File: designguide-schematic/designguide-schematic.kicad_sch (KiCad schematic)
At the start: 93 parts, among them J1 HRO_TYPE-C-31-M-14, J2 UDB, J3 Battery, J4 Battery, J5 Thermistor, J6 Battery, J7 SWD_TC2030, J8 SWD_TC2030, Q1 AO3401A, Q2 2N7002, Q3 AO3401A, Q4 2N7002, SW1 PWR, SW2 PWR, SW3 RESET, SW4 RESET, SW5 Keyswitch, SW6 Keyswitch, SW7 Keyswitch, SW8 Keyswitch, U1 SRV05-4, U10 TXB0101, U2 TP4056, U3 BQ24075, U4 DW01A, U5 FS8205, U6 XC6206PxxxMR, U7 nRF52840_holyiot_18010, U8 nRF52840_moko_mk08, U9 MAX17048

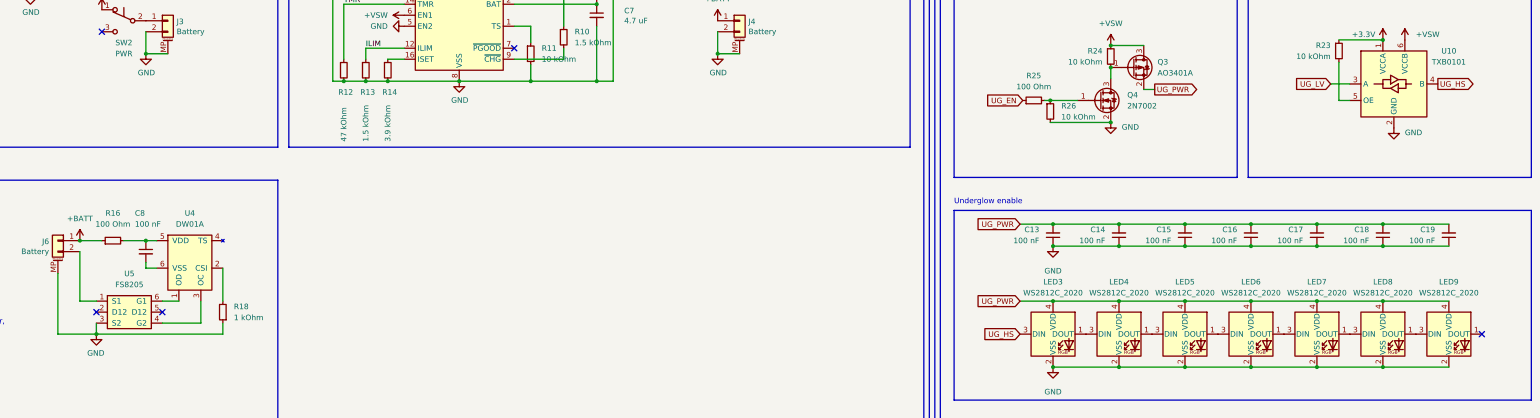
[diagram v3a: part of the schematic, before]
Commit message: fixed missing connection in batt protections, add disclaimer to readme
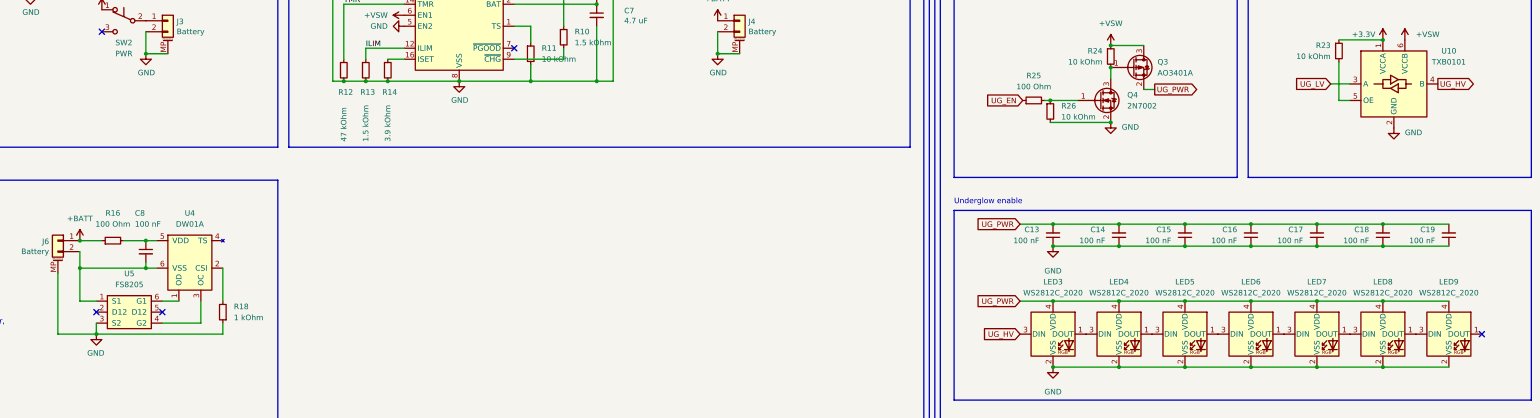
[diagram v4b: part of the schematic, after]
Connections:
- net at C8.2, U4.6 (VSS): now also J6.2 (Pin_2), U5.1 (S1)
- net UG_HS renamed UG_HV
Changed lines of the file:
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@@
   (junction (at 36.83 256.54) (diameter 0) (color 0 0 0 0)
   )
+  (junction (at 80.01 185.42) (diameter 0) (color 0 0 0 0)
+  )
   (junction (at 335.28 193.04) (diameter 0) (color 0 0 0 0)
   )
@@
   )
   (junction (at 227.33 110.49) (diameter 0) (color 0 0 0 0)
+  )
+  (junction (at 95.25 185.42) (diameter 0) (color 0 0 0 0)
   )
   (junction (at 151.13 142.24) (diameter 0.9144) (color 0 0 0 0)
@@
     (stroke (width 0) (type default) (color 0 0 0 0))
   )
+  (wire (pts (xy 80.01 185.42) (xy 95.25 185.42))
+    (stroke (width 0) (type default) (color 0 0 0 0))
+  )
   (polyline (pts (xy 281.94 215.9) (xy 415.29 215.9))
     (stroke (width 0) (type solid) (color 0 0 0 0))
@@
     (stroke (width 0) (type default) (color 0 0 0 0))
   )
+  (wire (pts (xy 80.01 185.42) (xy 80.01 193.04))
+    (stroke (width 0) (type default) (color 0 0 0 0))
+  )
   (wire (pts (xy 350.52 180.34) (xy 365.76 180.34))
     (stroke (width 0) (type default) (color 0 0 0 0))
@@
     (stroke (width 0) (type default) (color 0 0 0 0))
   )
-  (wire (pts (xy 80.01 181.61) (xy 80.01 193.04))
+  (wire (pts (xy 80.01 181.61) (xy 80.01 185.42))
     (stroke (width 0) (type default) (color 0 0 0 0))
   )
@@
     )
   )
-  (global_label "UG_HS" (shape output) (at 393.7 142.875 0) (fields_autoplaced)
-    (effects (font (size 1.27 1.27)) (justify left))
-    (property "Intersheet References" "${INTERSHEET_REFS}" (id 0) (at 402.2212 142.7956 0)
+  (global_label "UG_HV" (shape output) (at 393.7 142.875 0) (fields_autoplaced)
+    (effects (font (size 1.27 1.27)) (justify left))
+    (property "Intersheet References" "${INTERSHEET_REFS}" (id 0) (at 402.1002 142.7956 0)
       (effects (font (size 1.27 1.27)) (justify left) hide)
     )
@@
     )
   )
-  (global_label "UG_HS" (shape input) (at 297.18 200.66 180) (fields_autoplaced)
-    (effects (font (size 1.27 1.27)) (justify right))
-    (property "Intersheet References" "${INTERSHEET_REFS}" (id 0) (at 288.6588 200.5806 0)
-      (effects (font (size 1.27 1.27)) (justify right) hide)
-    )
+  (global_label "UG_HV" (shape input) (at 297.18 200.66 180) (fields_autoplaced)
+    (effects (font (size 1.27 1.27)) (justify right))
+    (property "Intersheet References" "${INTERSHEET_REFS}" (id 0) (at 288.7798 200.5806 0)
+      (effects (font (size 1.27 1.27)) (justify right) hide)
+    )

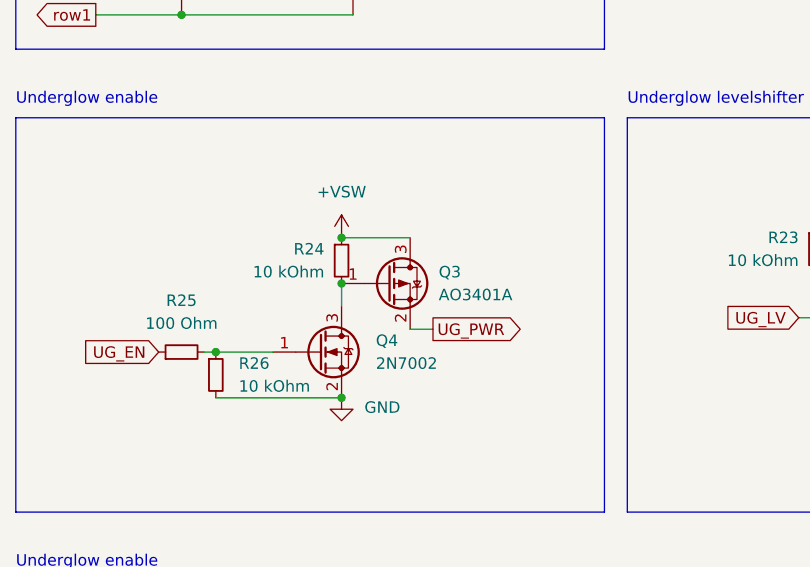
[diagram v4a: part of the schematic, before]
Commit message: fixed wrong rotation of p-ch FET in underglow supply
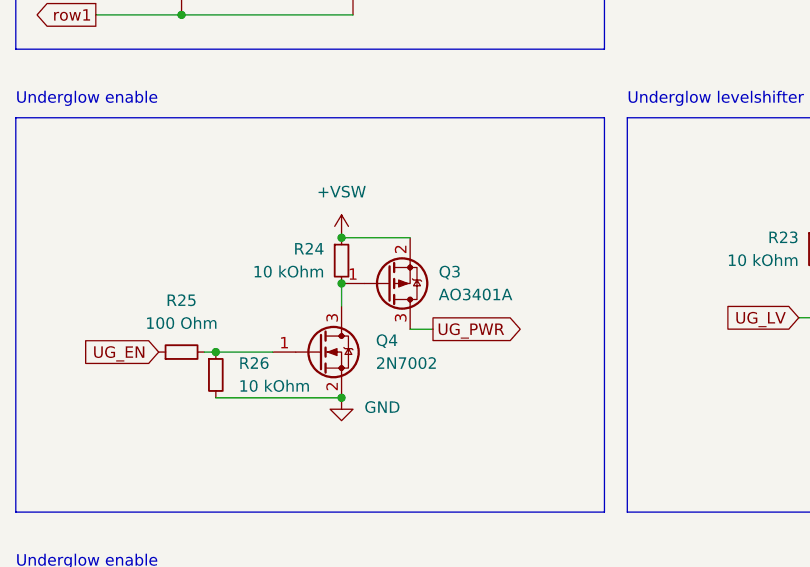
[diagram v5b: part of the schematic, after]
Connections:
- net +VSW: now also Q3.2 (S); no longer Q3.3 (D)
- net UG_PWR: now also Q3.3 (D); no longer Q3.2 (S)
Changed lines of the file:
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@@
   (junction (at 27.94 67.31) (diameter 0.9144) (color 0 0 0 0)
   )
+  (junction (at 318.135 139.065) (diameter 0) (color 0 0 0 0)
+  )
   (junction (at 350.52 175.26) (diameter 0) (color 0 0 0 0)
   )
@@
   )
   (junction (at 59.055 248.92) (diameter 0) (color 0 0 0 0)
-  )
-  (junction (at 318.135 139.065) (diameter 0) (color 0 0 0 0)
   )
   (junction (at 71.12 114.3) (diameter 0) (color 0 0 0 0)
@@
     (pin "2")
   )
-  (symbol (lib_id "Transistor_FET:AO3401A") (at 323.215 139.065 0) (unit 1)
+  (symbol (lib_id "Transistor_FET:AO3401A") (at 323.215 139.065 0) (mirror x) (unit 1)
     (in_bom yes) (on_board yes) (fields_autoplaced)
     (property "Reference" "Q3" (id 0) (at 328.93 137.7949 0)
@@
       (effects (font (size 1.27 1.27)) (justify left))
     )
-    (property "Footprint" "Package_TO_SOT_SMD:SOT-23" (id 2) (at 328.295 140.97 0)
+    (property "Footprint" "Package_TO_SOT_SMD:SOT-23" (id 2) (at 328.295 137.16 0)
       (effects (font (size 1.27 1.27) italic) (justify left) hide)
     )

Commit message: fixes #9, moves the project over to KiCad 7.0 and marbastlib PCM version instead of submodule
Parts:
- J7, J8: value SWD_TC2030 -> TC2030_SWD; footprint marbastlib-various:CON_TC2030_outlined -> PCM_marbastlib-various:CON_TC2030_outlined; symbol marbastlib-various:JTAG_TC2030 -> PCM_marbastlib-various:TC2030_SWD
- LED3, LED4, LED5, LED6, LED7, LED8, LED9: value WS2812C_2020 -> WS2812_2020; footprint marbastlib-various:LED_WS2812_2020 -> PCM_marbastlib-various:LED_WS2812_2020; symbol marbastlib-various:WS2812_2020 -> PCM_marbastlib-various:WS2812_2020
- SW1, SW2: footprint marbastlib-various:SW_MSK12C02-HB -> PCM_marbastlib-various:SW_MSK12C02-HB
- SW3, SW4: footprint (none) -> PCM_marbastlib-various:SW_SPST_SKQG_WithStem
- SW5, SW6, SW7, SW8: value Keyswitch -> MX_SW_HS; footprint (none) -> PCM_marbastlib-mx:SW_MX_HS_1u; symbol Switch:SW_Push_45deg -> PCM_marbastlib-mx:MX_SW_HS
- U10: symbol marbastlib-various:TXB0101 -> PCM_marbastlib-various:TXB0101
- U2: symbol marbastlib-various:TP4056 -> PCM_marbastlib-various:TP4056
- U4: symbol marbastlib-various:DW01A -> PCM_marbastlib-various:DW01A
- U5: symbol marbastlib-various:FS8205 -> PCM_marbastlib-various:FS8205
- U7: footprint marbastlib-various:nRF52840_holyiot_18010 -> PCM_marbastlib-various:nRF52840_holyiot_18010; symbol marbastlib-various:nRF52840_holyiot_18010 -> PCM_marbastlib-various:nRF52840_holyiot_18010
- U8: footprint marbastlib-various:nRF52840_moko_mk08 -> PCM_marbastlib-various:nRF52840_moko_mk08; symbol marbastlib-various:nRF52840_moko_mk08 -> PCM_marbastlib-various:nRF52840_moko_mk08
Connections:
- net USB-Di- is gone; now on net USB-D-: U1.1 (IO1)
- net USB-Do- is gone; now on net USB-D+: U1.6 (IO4)
- net GND: no longer U7.25 (GND)
- net SCL: now also R20.1; no longer R19.1
- net SDA: now also R19.1; no longer R20.1
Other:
- moved on the sheet: C12, D3, D4, D5, D6, Q3, Q4, R19, R20, R23, R24, R25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

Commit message: Address issue #10, add ebyte e73 module, add thermistor for bq24075, rework USB filtering to follow USB specs
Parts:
- removed R3: 1 MOhm, Resistor_SMD:R_0402_1005Metric, symbol Device:R_Small
- added C12: 1u, Capacitor_SMD:C_0402_1005Metric, symbol Device:C_Small
- added C13, C14: 4u7, Capacitor_SMD:C_0402_1005Metric, symbol Device:C_Small
- added C15, C16: 12p, Capacitor_SMD:C_0402_1005Metric, symbol Device:C_Small
- added J10: TC2030_SWD, PCM_marbastlib-various:CON_TC2030_outlined, symbol PCM_marbastlib-various:TC2030_SWD
- added J7: Thermistor, Connector_JST:JST_PH_S2B-PH-K_1x02_P2.00mm_Horizontal, symbol Connector_Generic_MountingPin:Conn_01x02_MountingPin
- added L3: 10 uH, Inductor_SMD:L_0603_1608Metric, symbol Device:L_Small
- added SW5: RST, PCM_marbastlib-various:SW_SPST_SKQG_WithStem, symbol Switch:SW_Push_45deg
- added U9: nRF52840_E73-2G4M08S1C, PCM_marbastlib-various:nRF52840_E73-2G4M08S1C, symbol PCM_marbastlib-various:nRF52840_E73-2G4M08S1C
- added Y1: 32.768 KHz, Crystal:Crystal_SMD_2012-2Pin_2.0x1.2mm, symbol Device:Crystal_Small
- C1, C11, C8: value 100 nF -> 100n
- C10, C9: value 1 uF -> 1u
- C17: renamed from C12; value 100 nF -> 100n; LCSC C52923 -> (none)
- C18: renamed from C13; value 100 nF -> 100n; LCSC C52923 -> (none)
- C19: renamed from C14; value 100 nF -> 100n; LCSC C52923 -> (none)
- C2, C4: value 10 uF -> 10u
- C20: renamed from C15; value 100 nF -> 100n; LCSC C52923 -> (none)
- C21: renamed from C16; value 100 nF -> 100n; LCSC C52923 -> (none)
- C22: renamed from C17; value 100 nF -> 100n; LCSC C52923 -> (none)
- C23: renamed from C18; value 100 nF -> 100n; LCSC C52923 -> (none)
- C24: renamed from C19; value 100 nF -> 100n; LCSC C52923 -> (none)
- C3, C5, C6, C7: value 4.7 uF -> 4u7
- J3: renamed from J4; footprint Connector_JST:JST_PH_S2B-PH-K_1x02_P2.00mm_Horizontal -> PCM_marbastlib-various:Molex_Pico-EZmate_78171-0002_1x02-1MP_P1.20mm_Vertical; LCSC (none) -> C505023
- J4: renamed from J3; footprint Connector_JST:JST_PH_S2B-PH-K_1x02_P2.00mm_Horizontal -> PCM_marbastlib-various:Molex_Pico-EZmate_78171-0002_1x02-1MP_P1.20mm_Vertical; LCSC (none) -> C505023
- J6: footprint Connector_JST:JST_PH_S2B-PH-K_1x02_P2.00mm_Horizontal -> PCM_marbastlib-various:Molex_Pico-EZmate_78171-0002_1x02-1MP_P1.20mm_Vertical; LCSC (none) -> C505023
- R1, R2: value 5.1 kOhm -> 5k1
- R10: value 1.5 kOhm -> 1k5
- R11: renamed from R12; value 47 kOhm -> 47k
- R12: renamed from R13; value 1.5 kOhm -> 1k5
- R13: renamed from R14; value 3.9 kOhm -> 3k9
- R14: renamed from R15; value 5 kOhm -> 5k
- R15: renamed from R16; value 100 Ohm -> 100R
- R16: renamed from R17; value 5 kOhm -> 5k
- R17: renamed from R18; value 1 kOhm -> 1k
- R18: renamed from R19; value 5.1 kOhm -> 5k1
- R19: renamed from R20; value 5.1 kOhm -> 5k1
- R20: renamed from R21; value 806 kOhm -> 806k
- R21: renamed from R22; value 2 MOhm -> 2M
- R22: renamed from R23; value 10 kOhm -> 10k
- R23: renamed from R24; value 10 kOhm -> 10k
- R24: renamed from R25; value 100 Ohm -> 100R
- R25: renamed from R26; value 10 kOhm -> 10k
- R3: renamed from R4; value 100 kOhm -> 100k
- R4: renamed from R5; value 100 Ohm -> 100R
- R5: renamed from R6; value 1.5 kOhm -> 1k5
- R6: renamed from R7; value 1.5 kOhm -> 1k5
- R7: renamed from R8; value 10 kOhm -> 10k
- R8: renamed from R9; value 5 kOhm -> 5k
- R9: renamed from R11; value 10 kOhm -> 10k
- SW3, SW4: value RESET -> RST
- SW6: renamed from SW5; footprint PCM_marbastlib-mx:SW_MX_HS_1u -> PCM_marbastlib-mx:SW_MX_HS_CPG151101S11_1u
- SW7: renamed from SW6; footprint PCM_marbastlib-mx:SW_MX_HS_1u -> PCM_marbastlib-mx:SW_MX_HS_CPG151101S11_1u
- SW8: renamed from SW7; footprint PCM_marbastlib-mx:SW_MX_HS_1u -> PCM_marbastlib-mx:SW_MX_HS_CPG151101S11_1u
- SW9: renamed from SW8; footprint PCM_marbastlib-mx:SW_MX_HS_1u -> PCM_marbastlib-mx:SW_MX_HS_CPG151101S11_1u
- renumbered J2 to J1, J1 to J2, J7 to J8, J8 to J9, U9 to U10, U10 to U11
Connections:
- net +3.3V: now also C12.1, J10.1 (VCC), L3.2, U9.19 (VDD)
- net +5V: now also C13.1, U9.27 (VBUS)
- net +VSW: now also C14.1, U9.23 (VDDH)
- net Earth: now also C1.1, D1.2 (A2), J2.A1 (GND), J2.A12 (GND), J2.B1 (GND), J2.B12 (GND), L2.1; no longer C1.2
- net GND: now also C1.2, D1.1 (A1), U7.25 (GND), C12.2, C13.2, C14.2, C15.2, C16.2, J10.5 (GND), J7.2 (Pin_2), J7.MP (MountPin), SW5.2, U9.21 (GND), U9.24 (GND), U9.5 (GND); no longer D1.2 (A2)
- net GNDPWR: no longer C1.1, D1.1 (A1), J2.A1 (GND), J2.A12 (GND), J2.B1 (GND), J2.B12 (GND), L2.1
- net RST: now also J10.3 (~{RST}), SW5.1, U9.26 (P0.18/~{RESET})
- net SCL: now also U9.15 (P0.05/AIN3)
- net SDA: now also U9.22 (P0.07)
- net SWDCLK: now also J10.4 (SWCLK), U9.39 (SWDCLK)
- net SWDIO: now also J10.2 (SWDIO), U9.37 (SWDIO)
- net UG_EN: now also U7.27 (P1.00), U8.49 (P1.00), U9.36 (P1.00); no longer U7.36 (P0.10-LF-NFC), U8.18 (P0.10-LF-NFC)
- net UG_LV: now also U7.26 (P0.22), U8.31 (P0.22), U9.34 (P0.22); no longer U7.35 (P0.09-LF-NFC), U8.17 (P0.09-LF-NFC)
- net USB-D+: now also U9.31 (D+)
- net USB-D-: now also U9.29 (D-)
- net col0: now also U8.2 (P0.02-LF-A), U9.7 (P0.02/AIN0); no longer U8.31 (P0.22)
- net col1: now also U8.3 (P0.28-LF-A), U9.4 (P0.28/AIN4); no longer U8.32 (P0.23)
- net row0: now also U8.4 (P0.29-LF-A), U9.8 (P0.29/AIN5); no longer U8.33 (P0.24)
- net row1: now also U8.5 (P0.30-LF-A), U9.10 (P0.30/AIN6); no longer U8.34 (P0.25)
- net TEMP renamed TEMP1
- net TEMP1: now also J7.1 (Pin_1)
- new net: C15.1, U9.11 (P0.00/XL1), Y1.2
- new net: C16.1, U9.13 (P0.01/XL2), Y1.1
- new net DCCH: L3.1, U9.25 (DCCH)
- no-connect marks 12 -> 13
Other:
- note added: "External DCCH inductor for DC-DC HV input mode"
- note added: "External LF crystal for lower idle power"
- note added: "MCU section (ebyte E73-2G4M08S1C)"
- note added: "Overtemperature protection (BQ24075) Use a 10k thermistor"
- note added: "Overtemperature protection (TP4056) For values of R15/R16 as well as the thermistor, refer to the datasheet."
- note added: "Underglow LEDs"
- note removed: "Overtemperature protection (TP4056 only) For values of R15/R16 as well as the Thermistor, refer to the datasheet."
- moved on the sheet: C17, C18, C19, C20, C21, C22, C23, C24, D1, D3, D4, D5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
